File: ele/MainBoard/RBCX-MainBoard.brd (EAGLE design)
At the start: 100 x 100 mm, 449 parts, among them IC1 AMS1117-3.3, IC10 INA180A4, IC11 INA180A4, IC12 MPU-6050, IC13 STM32F103VCT6, IC2 DRV8833PWP, IC3 INA180A4, IC4 INA180A4, IC5 DRV8833PWP, IC6 INA180A4, IC7 INA180A4, IC8 INA180A4, IC9 INA180A4, P1 M1, P2 M2, P3 M3, P4 M4, Q1 NCE20P45Q, Q10 2N7002, Q2 NCE20P45Q, Q3 2N7002, Q4 2N7002, Q5 2N7002, Q6 2N7002, Q7 2N7002, Q8 2N7002, Q9 2N7002, X1 POWER_IN, X2 POWER_OUT, X3 52559-3092, X4 uUSB, Y1 5032/2P, Y2 3215_2P

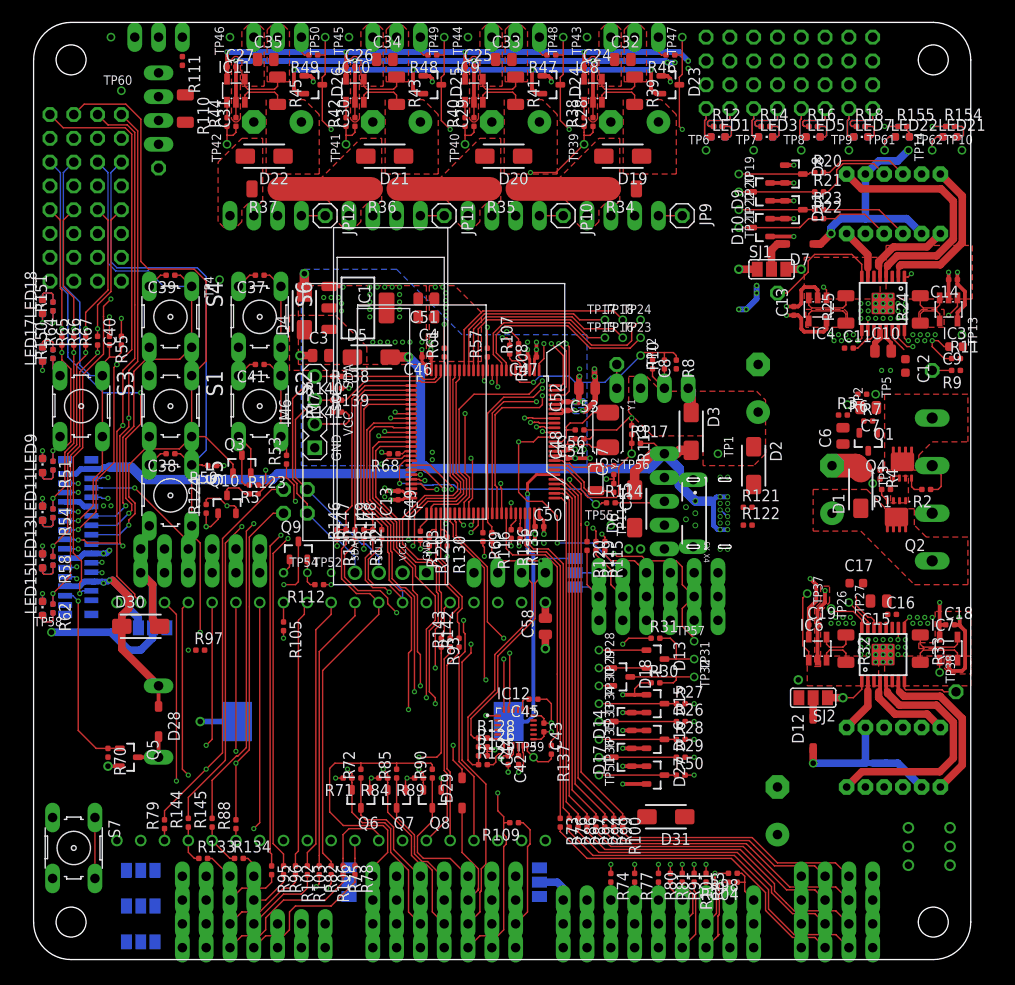
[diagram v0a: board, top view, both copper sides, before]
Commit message: MainBoard: Fix USB connectors, ROUTED
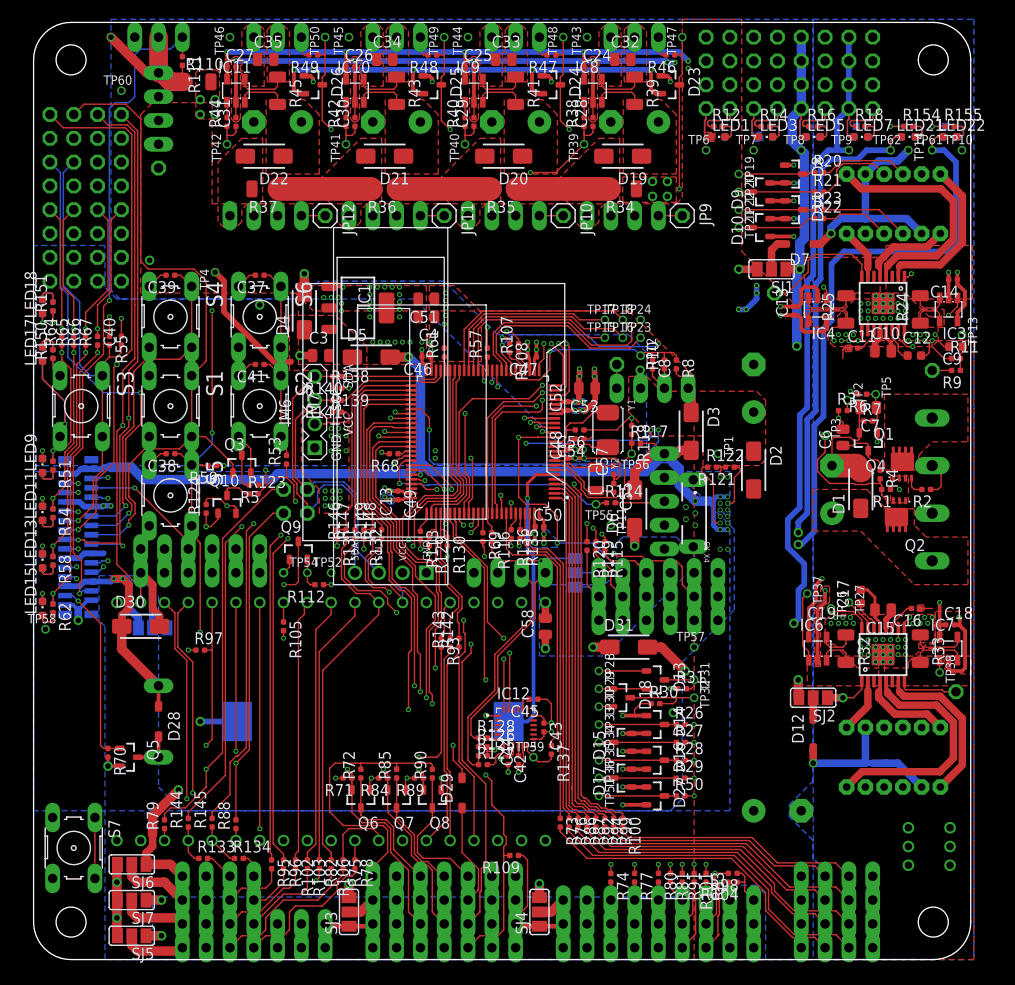
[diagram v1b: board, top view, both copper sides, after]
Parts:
- moved D31 18.5 mm to (63.5, 33.3), turned to 0 degrees
- moved R122 7.27 mm to (72.4, 52.5)
- moved TP3 7.18 mm to (84.5, 55.9)
- moved R31 6.11 mm to (69.2, 28.9)
- moved D15 5.41 mm to (62.9, 23.2), turned to 90 degrees
- moved LED22 5.08 mm to (97.8, 87.8)
- moved LED24 5.08 mm to (97.8, 87.8)
- moved R155 5.08 mm to (97.8, 88.9)
- moved R157 5.08 mm to (97.8, 88.9)
- moved TP61 5.08 mm to (95.9, 86.4)
- moved R121 4.69 mm to (74.3, 52.5), turned to 180 degrees
- moved LED21 4.45 mm to (93.3, 87.8)
- moved LED23 4.45 mm to (93.3, 87.8)
- moved R154 4.45 mm to (93.3, 88.9)
- moved R156 4.45 mm to (93.3, 88.9)
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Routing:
- net +3V3S: track 394.7 -> 538.3 mm, vias 74 -> 97
- net +3V3: track 42.0 -> 134.6 mm, vias 5 -> 8
- net GND_SEPARATOR: track 0.00 -> 83.5 mm
- net ESP_+5V: track 6.28 -> 86.1 mm, vias 2 -> 3
- net BUTTON-ON: track 74.5 -> 149.4 mm, vias 1 -> 4
- net VCC: track 11.8 -> 82.1 mm, vias 1 -> 3
- net POWER: track 0.00 -> 64.4 mm, vias 0 -> 3
- net V_BAT/2: track 0.00 -> 59.3 mm, vias 0 -> 2
- net VUSB: track 111.3 -> 168.1 mm, vias 1 -> 2
- net GND: track 534.9 -> 574.7 mm, vias 138 -> 133
- net +5V: track 42.4 -> 61.8 mm, vias 5 -> 18
- net ILED_PWR: track 0.00 -> 15.7 mm
- net 3V3_IN: track 0.27 -> 14.3 mm
- net BAT+_PROTECTED: track 0.00 -> 12.9 mm, vias 0 -> 1
- net PWRSW_GATE: track 1.45 -> 14.1 mm
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- added copper zone on layer 16, net +3V3
- added copper zone on layer 2, net +3V3
- added copper zone on layer 1, net +5V
- added copper zone on layer 16, net +5V
- added copper zone on layer 2, net ESP-I2C-PWR
- added copper zone on layer 16, net ESP_+5V

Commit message: MainBoardBRD: Fix DRC errors
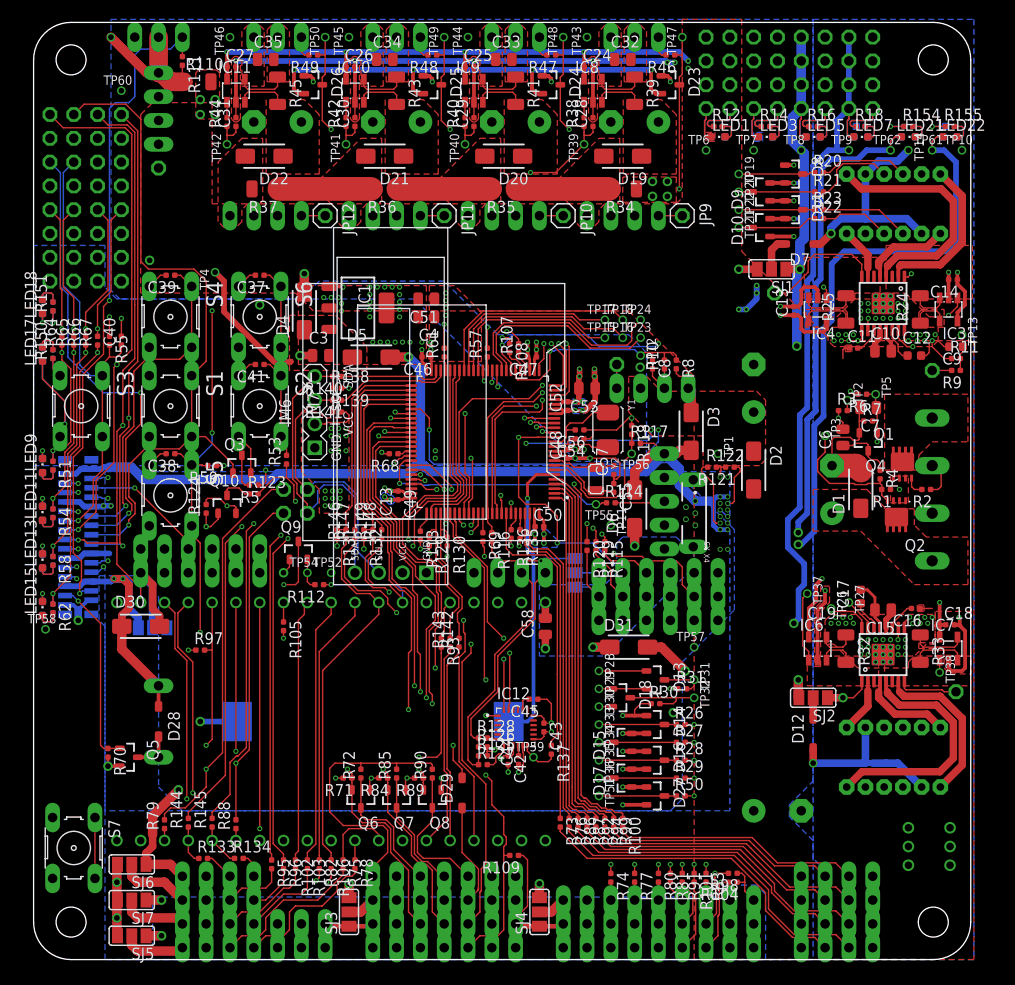
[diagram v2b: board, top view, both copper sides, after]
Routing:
- net GND: track 574.7 -> 558.2 mm
- net GND_SEPARATOR: track 83.5 -> 80.8 mm

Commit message: MainBoardBRD: Add isolation cutout polygon around analog ground vias
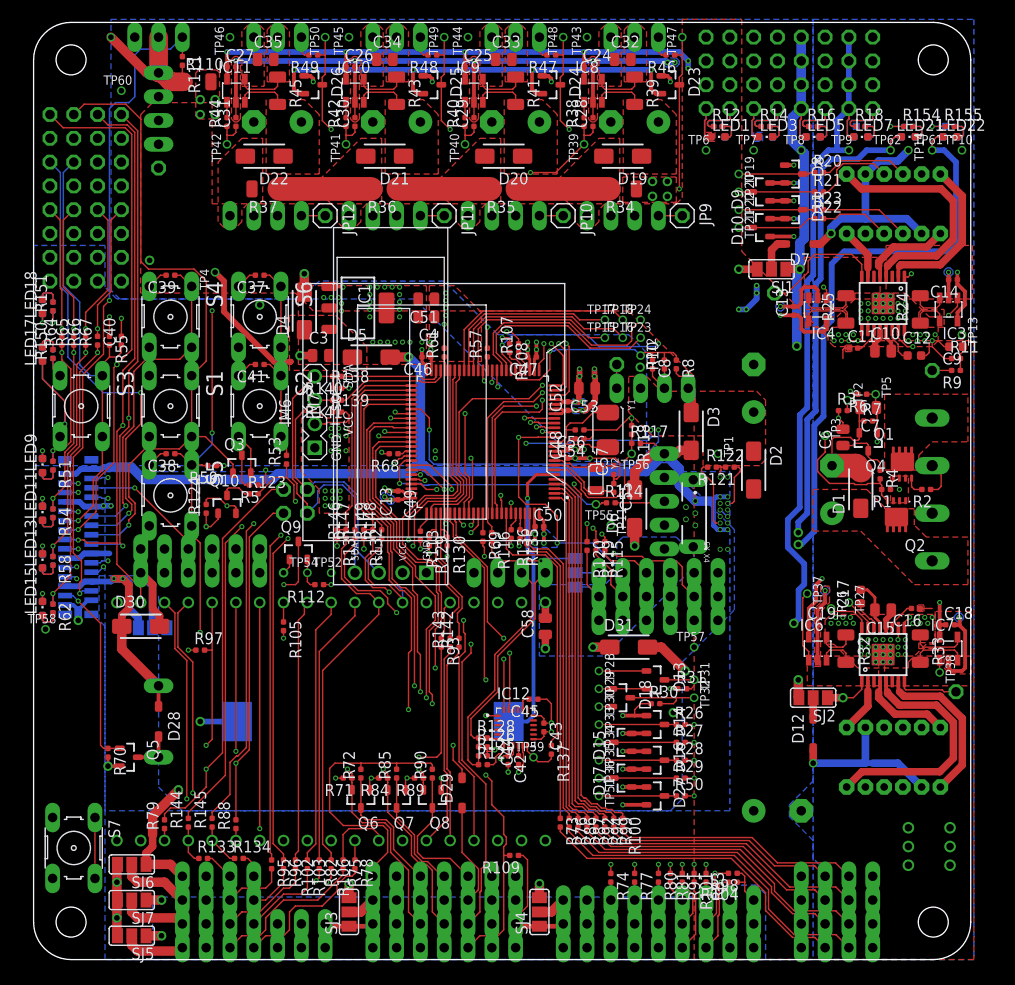
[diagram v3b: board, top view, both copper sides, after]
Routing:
- net +3V3S: track 538.5 -> 539.3 mm
- net VUSB_DET: track 16.5 -> 15.7 mm
- net ENC34PWR: track 18.8 -> 18.0 mm
- net +5V: track 61.8 -> 61.3 mm

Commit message: MainBoardSCH: Reorder sheets and renumber parts
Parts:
- removed C58: 10u, rcl_upravena:C0805
- added C5: 10u, rcl_upravena:C0805
- C10, C32, C33, C34, C35, C7: value 10u -> 1u; device rcl_upravena:C0805 -> rcl_upravena:C0402
- C11: value 10n -> 1u
- C12, C9: value 2u2 -> 1u; device rcl_upravena:C0603 -> rcl_upravena:C0402
- C13: value 100n -> 1u
- C14, C19: value 100n -> 10u; device rcl_upravena:C0402 -> rcl_upravena:C0805
- C15: value 10u -> 10n; device rcl_upravena:C0805 -> rcl_upravena:C0402
- C16: value 10n -> 2u2; device rcl_upravena:C0402 -> rcl_upravena:C0603
- C17: value 2u2 -> 100n; device rcl_upravena:C0603 -> rcl_upravena:C0402
- C20: value 220u -> 10n; device rcl_upravena:E5-10,5 -> rcl_upravena:C0402
- C21: value 220u -> 2u2; device rcl_upravena:E5-10,5 -> rcl_upravena:C0603
- C22, C23: value 220u -> 100n; device rcl_upravena:E5-10,5 -> rcl_upravena:C0402
- C24, C25, C26, C27: value 100n -> 220u; device rcl_upravena:C0402 -> rcl_upravena:E5-10,5
- C28, C29, C30, C31: value 1u -> 100n
- C36: value 220u -> 10u; device rcl_upravena:E5-10,5 -> rcl_upravena:C0805
- C37, C38, C39, C41: value 1u -> 10u; device rcl_upravena:C0402 -> rcl_upravena:C0805
- C40: value 1u -> 220u; device rcl_upravena:C0402 -> rcl_upravena:E5-10,5
- C8: value 1u -> 2u2; device rcl_upravena:C0402 -> rcl_upravena:C0603
- D10, D15, D9: value BAS40-04 -> B5819W; device diode:SOT23 -> diode:SOD123
- D12, D28, D29: value B5819W -> BAS40-04; device diode:SOD123 -> diode:SOT23
- D13, D18: value BAS40-05 -> BAS40-04
- D16: value BAS40-04 -> BAS40-05
- D19, D20, D30: value SS34 -> BAS40-04; device diode:SMA -> diode:SOT23
- D21: value SS34 -> BAS40-05; device diode:SMA -> diode:SOT23
- D23, D24, D25, D8: value BAS40-04 -> SS34; device diode:SOT23 -> diode:SMA
- IM3: value STEPDOWN -> DISPLAY-OLED-128X64-I2C-W_HOLES; device StepDown:STEPDOWN -> diy-modules:DISPLAY-OLED-128X64-I2C_W-HOLES
- IM4: value STEPDOWN -> DISPLAY-OLED-128X32; device StepDown:STEPDOWN -> diy-modules:DISPLAY-OLED-128X32
- IM6: value DISPLAY-OLED-128X64-I2C-W_HOLES -> STEPDOWN; device diy-modules:DISPLAY-OLED-128X64-I2C_W-HOLES -> StepDown:STEPDOWN
- IM7: value DISPLAY-OLED-128X32 -> STEPDOWN; device diy-modules:DISPLAY-OLED-128X32 -> StepDown:STEPDOWN
- JP10: value SERVO2_EN -> ESP_I2C1_5V; device pinhead:1X01 -> pinhead:1X04
- JP11: value SERVO3_EN -> ESP_UART_AUX; device pinhead:1X01 -> pinhead:1X03
- JP12: value SERVO4_EN -> ESP_I2C_AUX1_5V; device pinhead:1X01 -> pinhead:1X03
- JP13: value SERVO1 -> ESP_SPI_AUX1
- JP14: value SERVO2 -> UTS2; device pinhead:1X03 -> pinhead:1X04
- JP15: value SERVO3 -> ESP_I2C2_5V; device pinhead:1X03 -> pinhead:1X04
- JP16: value SERVO4 -> ESP_SPI2; device pinhead:1X03 -> pinhead:1X06
- JP17: value INTELIGENT_SERVO1 -> UTS3; device iServo_connector:292161-3 -> pinhead:1X04
- JP18: value INTELIGENT_SERVO2 -> STM_UART; device iServo_connector:292161-3 -> pinhead:1X04
- JP19: value BUTTONS -> ESP_I2C_AUX2_5V; device pinhead:2X04 -> pinhead:1X03
- JP20: value LEDS -> ESP_SPI_AUX2; device pinhead:2X04 -> pinhead:1X03
- JP21: value PWR_BUTTONS -> UTS4; device pinhead:2X04 -> pinhead:1X04
- JP22: value ESP_UART -> ESP_SPI3; device pinhead:1X04 -> pinhead:1X06
- JP23: value UTS1 -> ESP_I2C1
- JP24: value ESP_SPI1 -> ESP_SPI_AUX3; device pinhead:1X06 -> pinhead:1X03
- JP25: value ESP_I2C1_5V -> ESP_UCOM
- JP26: value ESP_UART_AUX -> ESP_I2C_AUX1
- JP27: value ESP_I2C_AUX1_5V -> ESP_UCOM_AUX
- JP28: value ESP_SPI_AUX1 -> ESP_I2C2; device pinhead:1X03 -> pinhead:1X04
- JP29: value UTS2 -> IM9_EN; device pinhead:1X04 -> pinhead:1X01
- JP30: value ESP_I2C2_5V -> AIO; device pinhead:1X04 -> pinhead:2X04
- JP31: value ESP_SPI2 -> ESP_I2C_AUX2; device pinhead:1X06 -> pinhead:1X03
- JP32: value UTS3 -> ILED; device pinhead:1X04 -> pinhead:1X03
- JP33: value STM_UART -> USB; device pinhead:1X04 -> pinhead:1X05
- JP34: value ESP_I2C_AUX2_5V -> SWD; device pinhead:1X03 -> pinhead:1X06
- JP35: value ESP_SPI_AUX2 -> DEBUG; device pinhead:1X03 -> pinhead:1X04
- JP36: value UTS4 -> BOOT_SW; device pinhead:1X04 -> pinhead:1X02
- JP37: value ESP_SPI3 -> ESP32_JTAG
- JP38: value ESP_I2C1 -> MPU_I2C
- JP39: value ESP_SPI_AUX3 -> EXPANDER_UART; device pinhead:1X03 -> pinhead:1X06
- JP40: value ESP_UCOM -> ESP_PROG_UART
- JP41: value ESP_I2C_AUX1 -> EXPANDER_CAN/I2C; device pinhead:1X03 -> pinhead:1X06
- JP42: value ESP_UCOM_AUX -> BUTTONS; device pinhead:1X03 -> pinhead:2X04
- JP43: value ESP_I2C2 -> LEDS; device pinhead:1X04 -> pinhead:2X04
- JP44: value IM9_EN -> PWR_BUTTONS; device pinhead:1X01 -> pinhead:2X04
- JP45: value AIO -> M12FAULT; device pinhead:2X04 -> pinhead:1X01
- JP46: value ESP_I2C_AUX2 -> M34FAULT; device pinhead:1X03 -> pinhead:1X01
- JP47: value ILED -> SERVO1_EN; device pinhead:1X03 -> pinhead:1X01
- JP48: value USB -> SERVO2_EN; device pinhead:1X05 -> pinhead:1X01
- JP49: value SWD -> SERVO3_EN; device pinhead:1X06 -> pinhead:1X01
- JP50: value DEBUG -> SERVO4_EN; device pinhead:1X04 -> pinhead:1X01
- JP51: value BOOT_SW -> SERVO1; device pinhead:1X02 -> pinhead:1X03
- JP52: value ESP32_JTAG -> SERVO2; device pinhead:1X06 -> pinhead:1X03
- JP53: value MPU_I2C -> SERVO3; device pinhead:1X04 -> pinhead:1X03
- JP54: value EXPANDER_UART -> SERVO4; device pinhead:1X06 -> pinhead:1X03
- JP55: value ESP_PROG_UART -> INTELIGENT_SERVO1; device pinhead:1X04 -> iServo_connector:292161-3
- JP56: value EXPANDER_CAN/I2C -> INTELIGENT_SERVO2; device pinhead:1X06 -> iServo_connector:292161-3
- JP7: value M12FAULT -> ESP_UART; device pinhead:1X01 -> pinhead:1X04
- JP8: value M34FAULT -> UTS1; device pinhead:1X01 -> pinhead:1X04
- JP9: value SERVO1_EN -> ESP_SPI1; device pinhead:1X01 -> pinhead:1X06
- LED10, LED9: value green -> red
- LED11, LED12: value yellow -> red
- LED13, LED14: value red -> green
- LED15, LED16: value blue -> yellow
- LED19, LED20: value red -> blue
- R104, R98: value 100k -> 330R
- R109: value 4k7 -> 100k
- R110, R37: value 0R -> 4k7; device rcl_upravena:R1206 -> rcl_upravena:R0402
- R112, R113, R132, R134, R136, R76, R77: value 330R -> 1k
- R114: value 1k5 -> 2k2
- R115, R116, R120, R140, R141, R142, R143, R144: value 330R -> 2k2
- R117: value 5k6 -> 2k2
- R118: value 10k -> 5m; device rcl_upravena:R0402 -> rcl_upravena:R1206
- R119, R127, R133, R135, R137: value 330R -> 5m; device rcl_upravena:R0402 -> rcl_upravena:R1206
- R121, R122: value 1k -> 2k2
- R123: value 100k -> 2k2
- R124: value 100k -> 10k
- R125, R71: value 4k7 -> 10k
- R126, R139: value 4k7 -> 5m; device rcl_upravena:R0402 -> rcl_upravena:R1206
- R128, R129, R130, R131, R63: value 330R -> 0R; device rcl_upravena:R0402 -> rcl_upravena:R1206
- R138: value 4k7 -> 1k
- R150, R152, R72, R84, R85, R89, R90, R97: value 4k7 -> 330R
- R151, R153, R156, R157, R40, R44: value 1k -> 330R
- R154, R155, R38, R42: value 1k -> 4k7
- R20, R21, R22, R23: value 2k2 -> 1k
- R24, R25, R43: value 5m -> 4k7; device rcl_upravena:R1206 -> rcl_upravena:R0402
- R26, R27, R28, R29, R46, R47, R48, R49: value 2k2 -> 330R
- R30, R31: value 10k -> 330R
- R32, R33, R39, R41, R45: value 5m -> 330R; device rcl_upravena:R1206 -> rcl_upravena:R0402
- R34, R35, R36: value 0R -> 330R; device rcl_upravena:R1206 -> rcl_upravena:R0402
- R50: value 2k2 -> 4k7
- R51, R57, R74, R75: value 330R -> 100k
- R62, R64, R78, R79: value 330R -> 4k7
- R67: value 330R -> 1k5
- R70: value 100k -> 5k6
- moved JP32 117.1 mm to (13.3, 98.4), turned to 0 degrees
- moved JP21 113.3 mm to (85.7, 8.89)
- moved JP29 108.4 mm to (13.3, 84.5), turned to 90 degrees
- moved LED11 104.8 mm to (97.8, 87.8), turned to 270 degrees
- moved LED12 104.8 mm to (97.8, 87.8), turned to 90 degrees
- moved JP20 101.7 mm to (74.3, 3.81)
- moved TP46 101.6 mm to (96.7, 30.6), turned to 270 degrees
- moved JP16 101.5 mm to (62.9, 3.81), turned to 180 degrees
- moved JP14 100.6 mm to (85.7, 3.81), turned to 180 degrees
- moved LED22 99.6 mm to (0.95, 64.6), flipped to the bottom, turned to 0 degrees
- moved LED10 98.8 mm to (93.3, 87.8), turned to 90 degrees
- moved LED9 98.8 mm to (93.3, 87.8), turned to 270 degrees
- moved LED24 98.5 mm to (0.95, 69.7), turned to 0 degrees
- moved LED21 95.3 mm to (0.95, 64.6), turned to 0 degrees
- moved LED23 94.1 mm to (0.95, 69.7), flipped to the top, turned to 0 degrees
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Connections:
- net !M12_FAULT: now also JP45.1; no longer JP7.1
- net !M34_FAULT: now also JP46.1; no longer JP8.1
- net +3V3: now also JP11.3, JP13.3, JP16.1, JP20.3, JP22.1, JP23.1, JP24.3, JP27.3, JP28.1, JP31.3, JP37.5, Q5.1, R24.2, R37.2, R42.2, R50.1, R51.1, R57.1, R62.1, SJ1.1, SJ2.1, TP10.P$1; no longer JP28.3, JP31.1, JP35.3, JP37.1, JP38.1, JP39.3, JP41.3, JP42.3, JP43.1, JP46.3, JP52.5, Q8.1, R104.1, R109.1, R71.2, R84.2, R89.2, R97.1, R98.1, SJ4.1, SJ7.1, TP9.P$1
- net +3V3S: now also C17.1, C22.1, C23.1, C28.1, C29.1, C30.1, C31.1, D12.2, D13.2, D18.2, D19.2, D20.2, D28.2, D29.2, D30.2, IM3.2, IM4.2, JP30.5, JP30.6, JP34.1, JP35.1, JP36.1, JP38.1, JP40.1, LED23.A, LED24.A, Q8.1, R154.2, R155.2, R78.2, R79.2, SJ4.1, SJ7.1, SJ8.1, TP9.P$1; no longer C13.1, C14.1, C19.1, C24.1, C25.1, C26.1, C27.1, D10.2, D15.2, D16.2, D23.2, D24.2, D25.2, D8.2, D9.2, IM6.2, IM7.2, JP45.5, JP45.6, JP49.1, JP50.1, JP51.1, JP53.1, JP55.1, LED18.A, LED20.A, Q9.1, R125.2, R126.2, R138.2, R139.2, SJ1.1, SJ2.1, SJ6.1, TP8.P$1
- net +5V: now also D8.C, D9.C, JP14.1, JP17.1, JP21.1, JP30.7, JP30.8, JP8.1, R128.1, R63.2, SJ8.3, TP8.P$1; no longer D28.C, D30.C, JP23.1, JP29.1, JP32.1, JP36.1, JP45.7, JP45.8, R110.2, R34.1, SJ6.3, TP7.P$1
- net BOOT0: now also JP36.2, Q9.1, R75.1, TP19.P$1; no longer JP51.2, Q10.1, R124.1, TP57.P$1
- net BOOT1_PULL-DOWN: now also Q9.3, R74.1; no longer Q10.3, R123.1
- net BUTTON-1: now also C13.1, JP42.1, R92.2; no longer C41.1, JP19.1, R53.2
- net BUTTON-2: now also C12.1, JP42.3, R94.2; no longer C40.1, JP19.3, R55.2
- net BUTTON-3: now also C11.1, JP42.5, R96.2; no longer C39.1, JP19.5, R57.2
- net BUTTON-4: now also C10.1, JP42.7, R98.2; no longer C38.1, JP19.7, R59.2
- net BUTTON-OFF: now also C9.1, JP44.1, R100.2; no longer C37.1, JP21.1, R61.2
- net BUTTON-ON: now also C5.2, JP44.3; no longer C6.2, JP21.3
- net BUTTON1: now also R74.2, R92.1; no longer R123.2, R53.1
- net BUTTON2: now also R94.1; no longer R55.1
- net BUTTON3: now also R96.1; no longer R57.1
- net BUTTON4: now also R98.1; no longer R59.1
- net BUTTON_OFF: now also R100.1; no longer R61.1
- net BUZZER: now also R108.1; no longer R69.1
- net BUZZER-: now also D9.A, Q10.3; no longer D28.A, Q5.3
- net BUZZER-GATE: now also Q10.1, R108.2, R109.1, TP21.P$1; no longer Q5.1, R69.2, R70.1, TP52.P$1
- net DEBUG-RX: now also JP35.3, R72.2; no longer JP50.3, R119.2
- net DEBUG-TX: now also JP35.4, R73.2, SJ6.1; no longer JP50.4, R120.2, SJ8.1
- net DEBUG_RX: now also R72.1; no longer R119.1
- net DEBUG_TX: now also R73.1; no longer R120.1
- net ENC12PWR: now also D10.C, TP22.P$1; no longer D7.C, TP14.P$1
- net ENC12_PWR: now also D10.A, SJ8.2; no longer D7.A, SJ1.2
- net ENC1A: now also D12.3, R115.1, TP28.P$1; no longer D8.3, R20.1, TP19.P$1
- net ENC1B-SWO: now also R69.2, SJ6.3; no longer R116.2, SJ8.3
- net ENC1B/SWO: now also D11.3, R114.1, R69.1, TP27.P$1; no longer D9.3, R116.1, R21.1, TP20.P$1
- net ENC2A: now also D14.3, R117.1, TP30.P$1; no longer D10.3, R22.1, TP21.P$1
- net ENC2B: now also D13.3, R116.1, TP29.P$1; no longer D11.3, R23.1, TP22.P$1
- net ENC34PWR: now also D15.C, TP33.P$1; no longer D12.C, TP25.P$1
- net ENC34_PWR: now also D15.A, SJ9.2; no longer D12.A, SJ2.2
- net ENC3A: now also D17.3, R120.1, TP41.P$1; no longer D14.3, R26.1, TP33.P$1
- net ENC3B: now also D18.3, R121.1, TP42.P$1; no longer D15.3, R27.1, TP34.P$1
- net ENC4A: now also D19.3, R122.1, TP43.P$1; no longer D16.3, R28.1, TP35.P$1
- net ENC4B: now also D20.3, R123.1, TP44.P$1; no longer D17.3, R29.1, TP36.P$1
- net ENC_1A: now also R115.2; no longer R20.2
- net ENC_1B: now also R114.2; no longer R21.2
- net ENC_2A: now also R117.2; no longer R22.2
- net ENC_2B: now also R116.2; no longer R23.2
- net ENC_3A: now also R120.2; no longer R26.2
- net ENC_3B: now also R121.2; no longer R27.2
- net ENC_4A: now also R122.2; no longer R28.2
- net ENC_4B: now also R123.2; no longer R29.2
- net ESP-EN: now also JP44.5, R107.2; no longer JP21.5, R68.2
- net ESP-I2C-PWR: now also JP10.1, JP12.3, JP15.1, JP19.3, R25.2, R38.2, R43.2, SJ1.2; no longer JP25.1, JP27.3, JP30.1, JP34.3, R72.2, R85.2, R90.2, SJ3.2
- net ESP-I2C-SCL: now also JP23.3, JP28.3, Q5.2, R24.1, R32.2; no longer JP38.3, JP43.3, Q6.2, R71.1, R79.2
- net ESP-I2C-SCL-5V: now also JP10.3, JP15.3, Q5.3, R25.1; no longer JP25.3, JP30.3, Q6.3, R72.1
- net ESP-I2C-SDA: now also JP23.4, JP28.4, Q6.2, R37.1, R41.2; no longer JP38.4, JP43.4, Q7.2, R84.1, R88.2
- net ESP-I2C-SDA-5V: now also JP10.4, JP15.4, Q6.3, R38.1; no longer JP25.4, JP30.4, Q7.3, R85.1
- net ESP-SPI-!CS1: now also JP9.6, R34.2; no longer JP24.6, R81.2
- net ESP-SPI-!CS2: now also JP16.6, R44.2; no longer JP31.6, R91.2
- net ESP-SPI-!CS3: now also JP22.6, R54.2; no longer JP37.6, R101.2
- net ESP-SPI-MISO: now also JP16.4, JP22.4, JP9.4, R30.2; no longer JP24.4, JP31.4, JP37.4, R77.2
- net ESP-SPI-MOSI: now also JP16.3, JP22.3, JP9.3, R27.2; no longer JP24.3, JP31.3, JP37.3, R74.2
- net ESP-SPI-SCK: now also JP16.5, JP22.5, JP9.5, R33.2; no longer JP24.5, JP31.5, JP37.5, R80.2
- net ESP-UART-RX: now also JP40.4, R87.2; no longer JP55.4, R134.2
- net ESP-UART-TX: now also JP40.3, R86.2; no longer JP55.3, R133.2
- net ESP-USART-RX: now also JP7.3, R28.2; no longer JP22.3, R75.2
- net ESP-USART-TX: now also JP7.4, R31.2; no longer JP22.4, R78.2
- net ESP_+5V: now also C41.2, LED11.A, LED12.A; no longer C58.2, LED22.A, LED24.A
- net ESP_COM_RX: now also R145.2, R83.1; no longer R130.1, R142.2
- net ESP_COM_TX: now also R146.2, R82.1; no longer R129.1, R143.2
- net ESP_EN: now also R107.1; no longer R68.1
- net ESP_PROG_RX: now also R147.2; no longer R144.2
- net ESP_PROG_TX: now also R148.2; no longer R145.2
- net ESP_SPI_PWR: now also JP9.1, SJ2.2; no longer JP24.1, SJ4.2
- net ESP_UCOM_PWR: now also JP25.1, SJ5.2; no longer JP40.1, SJ7.2
- net ESP_USART_PWR: now also JP7.1, SJ3.2; no longer JP22.1, SJ5.2
- net EXPANDER-COM-DIR: now also JP39.5, JP41.5, R84.2; no longer JP54.5, JP56.5, R131.2
- net EXPANDER-COM-INT: now also JP39.6, JP41.6, R85.2; no longer JP54.6, JP56.6, R132.2
- net EXPANDER-UART-RX: now also JP39.4, R83.2; no longer JP54.4, R130.2
- net EXPANDER-UART-TX: now also JP39.3, R82.2; no longer JP54.3, R129.2
- net EXPANDER_COM_PWR: now also D8.A, JP39.1, JP41.1, SJ7.2, TP20.P$1; no longer D30.A, JP54.1, JP56.1, SJ9.2, TP58.P$1
- net EXPANDER_RX: now also R146.1; no longer R143.1
- net EXPANDER_TX: now also R145.1; no longer R142.1
- net GND: now also C11.2, C16.2, C21.2, C22.2, C23.2, C24.-, C25.-, C26.-, C27.-, C32.2, C33.2, C34.2, C35.2, C36.1, C37.1, C38.1, C39.1, C40.-, C41.1, C6.2, D12.1, D13.1, D18.1, D19.1, D20.1, D28.1, D29.1, D30.1, IM3.1, IM4.1, IM6.GND, IM7.GND, JP10.2, JP11.2, JP12.2, JP13.2, JP14.4, JP15.2, JP16.2, JP17.4, JP18.2, JP23.2, JP30.3, JP30.4, JP32.3, JP33.5, JP34.3, JP37.6, JP42.4, JP42.6, JP42.8, JP43.4, JP43.6, JP43.8, JP44.2, JP44.4, JP44.6, JP44.8, JP51.3, JP52.3, JP53.3, JP54.3, JP55.3, JP56.3, JP7.2, JP8.4, JP9.2, LED17.C, LED18.C, LED19.C, LED20.C, Q9.2, R109.2, R110.1, R111.1, R112.1, R113.1, R119.1, R124.1, R125.1, R126.1, R127.1, R20.1, R21.1, R22.1, R23.1, R71.1, R75.2, R76.2, R77.2, TP11.P$1; no longer C15.2, C20.-, C21.-, C22.-, C23.-, C24.2, C25.2, C26.2, C27.2, C32.1, C33.1, C34.1, C35.1, C36.-, C37.2, C38.2, C39.2, C40.2, C41.2, C58.1, D10.1, D15.1, D16.1, D23.1, D24.1, D25.1, D8.1, D9.1, IM3.GND, IM4.GND, IM6.1, IM7.1, JP13.3, JP14.3, JP15.3, JP16.3, JP17.3, JP18.3, JP19.4, JP19.6, JP19.8, JP20.4, JP20.6, JP20.8, JP21.2, JP21.6, JP21.8, JP23.4, JP29.4, JP30.2, JP32.4, JP33.2, JP34.2, JP36.4, JP37.2, JP45.3, JP45.4, JP46.2, JP47.3, JP48.5, JP49.3, JP50.2, JP52.6, JP53.2, JP54.2, JP55.2, JP56.2, LED10.C, LED11.C, LED12.C, LED9.C, Q5.2, R121.2, R122.2, R124.2, R150.1, R151.1, R152.1, R153.1, R154.1, R155.1, R156.1, R157.1, R24.1, R25.1, R30.1, R31.1, R32.1, R33.1, R70.2, TP10.P$1
- net GPIO-1: now also JP13.1, R36.2; no longer JP28.1, R83.2
- net GPIO-1-5V: now also JP12.1, Q7.3, R43.1; no longer JP27.1, Q8.3, R90.1
- net GPIO-2: now also JP26.1, R58.2; no longer JP41.1, R105.2
- net GPIO-3: now also JP25.3, R55.2; no longer JP40.3, R102.2
- net GPIO-4: now also JP25.4, R56.2; no longer JP40.4, R103.2
- net GPIO-5: now also JP11.1, R35.2; no longer JP26.1, R82.2
- net GPIO-6: now also JP27.1, R59.2; no longer JP42.1, R106.2
- net GPIO-7: now also Q7.2, R42.1, R46.2; no longer Q8.2, R89.1, R93.2
- net GPIO1: now also R36.1; no longer R83.1
- net GPIO2: now also R58.1; no longer R105.1
- net GPIO3: now also R55.1; no longer R102.1
- net GPIO4: now also R56.1; no longer R103.1
- net GPIO5: now also R35.1; no longer R82.1
- net GPIO6/TMS: now also JP37.1, R149.1, R59.1; no longer JP52.1, R106.1, R146.1
- net GPIO7/TCK: now also JP37.3, R150.1, R46.1; no longer JP52.3, R147.1, R93.1
- net I2C_SCL: now also R32.1; no longer R79.1
- net I2C_SDA: now also R41.1; no longer R88.1
- net ILED: now also Q8.2, R65.2, TP16.P$1; no longer Q9.2, R112.2, TP54.P$1
- net ILED-5V: now also JP32.1, Q8.3, R64.1; no longer JP47.1, Q9.3, R111.1
- net ILED_PWR: now also IM2.OUT, JP32.2, R63.1, R64.2, TP15.P$1; no longer IM8.OUT, JP47.2, R110.1, R111.2, TP53.P$1
- net IM9_EN: now also IM2.EN, JP29.1; no longer IM8.EN, JP44.1
- net IN1: now also JP20.1, R51.2; no longer JP35.1, R98.2
- net IN2: now also JP24.1, R57.2; no longer JP39.1, R104.2
- net IN3: now also D7.A, R50.2; no longer D29.A, R97.2
- net IN3-5V: now also D7.C, JP19.1; no longer D29.C, JP34.1
- net IN4: now also JP31.1, R62.2; no longer JP46.1, R109.2
- net IN4A: now also D16.1, TP36.P$1; no longer D13.1, TP28.P$1
- net IN4B: now also D21.2, TP38.P$1; no longer D18.2, TP30.P$1
- net IN4_A: now also D16.3, R125.2, TP39.P$1; no longer D13.3, R31.2, TP31.P$1
- net IN4_B: now also D21.3, R124.2, TP40.P$1; no longer D18.3, R30.2, TP32.P$1
- net INTELLIGENT_SERVO: now also D30.3, R144.1, TP59.P$1; no longer D27.3, R50.1, TP51.P$1
- net ISERVO: now also JP55.1, JP56.1, R144.2; no longer JP17.1, JP18.1, R50.2
- net I_LED/TDI: now also JP37.2, R151.1, R65.1; no longer JP52.2, R112.1, R148.1
- net LED-1: now also JP43.1, R103.2; no longer JP20.1, R64.2
- net LED-2: now also JP43.3, R104.2; no longer JP20.3, R65.2
- net LED-3: now also JP43.5, R105.2; no longer JP20.5, R66.2
- net LED-4: now also JP43.7, R106.2; no longer JP20.7, R67.2
- net LED1: now also R103.1, R90.1, R91.1; no longer R51.1, R52.1, R64.1
- net LED2: now also R104.1, R93.1, R95.1; no longer R54.1, R56.1, R65.1
- net LED3: now also R105.1, R97.1, R99.1; no longer R58.1, R60.1, R66.1
- net LED4: now also R101.1, R102.1, R106.1; no longer R62.1, R63.1, R67.1
- net LED_1: now also LED13.A, R90.2; no longer LED9.A, R51.2
- net LED_1B: now also LED14.A, R91.2; no longer LED10.A, R52.2
- net LED_2: now also LED15.A, R93.2; no longer LED11.A, R54.2
- net LED_2B: now also LED16.A, R95.2; no longer LED12.A, R56.2
- net LED_3: now also LED17.A, R97.2; no longer LED13.A, R58.2
- net LED_3B: now also LED18.A, R99.2; no longer LED14.A, R60.2
- net LED_4: now also LED19.A, R101.2; no longer LED15.A, R62.2
- net LED_4B: now also LED20.A, R102.2; no longer LED16.A, R63.2
- net M1GND: now also R118.2; no longer R24.2
- net M2GND: now also R119.2; no longer R25.2
- net M3GND: now also R126.2; no longer R32.2
- net M4GND: now also R127.2; no longer R33.2
- net MI1: now also TP31.P$1; no longer TP23.P$1
- net MI2: now also TP32.P$1; no longer TP24.P$1
- net MI3: now also TP45.P$1; no longer TP37.P$1
- net MI4: now also TP46.P$1; no longer TP38.P$1
- net MPU-INT: now also R153.2, TP62.P$1; no longer R137.2, TP59.P$1
- net MPU-SCL: now also JP38.3, R78.1, R80.1; no longer JP53.3, R125.1, R127.1
- net MPU-SDA: now also JP38.4, R79.1, R81.1; no longer JP53.4, R126.1, R128.1
- net MPU_INT: now also R153.1; no longer R137.1
- net MPU_SCL: now also R80.2; no longer R127.2
- net MPU_SDA: now also R81.2; no longer R128.2
- net NRST: now also JP34.5, JP44.7; no longer JP21.7, JP49.5
- net POWER: now also C6.1, TP6.P$1; no longer C7.1, TP5.P$1
- net PWM1A: now also TP23.P$1; no longer TP15.P$1
- net PWM1B: now also TP24.P$1; no longer TP16.P$1
- net PWM2A: now also TP25.P$1; no longer TP17.P$1
- net PWM2B: now also TP26.P$1; no longer TP18.P$1
- net PWM3A: now also TP34.P$1; no longer TP26.P$1
- net PWM3B: now also TP35.P$1; no longer TP27.P$1
- net PWM4: now also D16.2, D21.1, TP37.P$1; no longer D13.2, D18.1, TP29.P$1
- net PWRLED_+3V3S1: now also LED23.C, R112.2; no longer LED18.C, R151.2
- net PWRLED_+3V3S_B1: now also LED24.C, R113.2; no longer LED20.C, R153.2
- net PWRLED_+5VESP: now also LED11.C, R22.2; no longer LED22.C, R155.2
- net PWRLED_+5VESP_B: now also LED12.C, R23.2; no longer LED24.C, R157.2
- net PWRLED_VCC1: now also LED21.C, R110.2; no longer LED17.C, R150.2
- net PWRLED_VCC_B1: now also LED22.C, R111.2; no longer LED19.C, R152.2
- net PWRLED_VUSB: now also LED9.C, R20.2; no longer LED21.C, R154.2
- net PWRLED_VUSB_B: now also LED10.C, R21.2; no longer LED23.C, R156.2
- net PWRSW: now also C5.1; no longer C6.1
- net SERVO1: now also D26.3, R140.1, TP55.P$1; no longer D23.3, R46.1, TP47.P$1
- net SERVO1PWR: now also D22.A, IM5.OUT, R128.2, R129.1; no longer D19.A, IM2.OUT, R34.2, R35.1
- net SERVO1_EN: now also IM5.EN, JP47.1; no longer IM2.EN, JP9.1
- net SERVO1_PWR: now also C24.+, D22.C, R133.2; no longer C20.+, D19.C, R39.2
- net SERVO2: now also D27.3, R141.1, TP56.P$1; no longer D24.3, R47.1, TP48.P$1
- net SERVO2PWR: now also D23.A, IM6.OUT, R129.2, R130.1; no longer D20.A, IM3.OUT, R35.2, R36.1
- net SERVO2_EN: now also IM6.EN, JP48.1; no longer IM3.EN, JP10.1
- net SERVO2_PWR: now also C25.+, D23.C, R135.2; no longer C21.+, D20.C, R41.2
- net SERVO3: now also D28.3, R142.1, TP57.P$1; no longer D25.3, R48.1, TP49.P$1
- net SERVO3PWR: now also D24.A, IM7.OUT, R130.2, R131.1; no longer D21.A, IM4.OUT, R36.2, R37.1
- net SERVO3_EN: now also IM7.EN, JP49.1; no longer IM4.EN, JP11.1
- net SERVO3_PWR: now also C26.+, D24.C, R137.2; no longer C22.+, D21.C, R43.2
- net SERVO4: now also D29.3, R143.1, TP58.P$1; no longer D26.3, R49.1, TP50.P$1
- net SERVO4PWR: now also D25.A, IM8.OUT, R131.2; no longer D22.A, IM5.OUT, R37.2
- net SERVO4_EN: now also IM8.EN, JP50.1; no longer IM5.EN, JP12.1
- net SERVO4_PWR: now also C27.+, D25.C, R139.2; no longer C23.+, D22.C, R45.2
- net SERVO_1: now also JP51.1, R140.2; no longer JP13.1, R46.2
- net SERVO_1_PWR: now also C36.2, JP51.2, R133.1, TP51.P$1; no longer C32.2, JP13.2, R39.1, TP43.P$1
- net SERVO_2: now also JP52.1, R141.2; no longer JP14.1, R47.2
- net SERVO_2_PWR: now also C37.2, JP52.2, R135.1, TP52.P$1; no longer C33.2, JP14.2, R41.1, TP44.P$1
- net SERVO_3: now also JP53.1, R142.2; no longer JP15.1, R48.2
- net SERVO_3_PWR: now also C38.2, JP53.2, R137.1, TP53.P$1; no longer C34.2, JP15.2, R43.1, TP45.P$1
- net SERVO_4: now also JP54.1, R143.2; no longer JP16.1, R49.2
- net SERVO_4_PWR: now also C39.2, JP54.2, R139.1, TP54.P$1; no longer C35.2, JP16.2, R45.1, TP46.P$1
- net SI1: now also C32.1, R132.1, TP47.P$1; no longer C28.1, R38.1, TP39.P$1
- net SI2: now also C33.1, R134.1, TP48.P$1; no longer C29.1, R40.1, TP40.P$1
- net SI3: now also C34.1, R136.1, TP49.P$1; no longer C30.1, R42.1, TP41.P$1
- net SI4: now also C35.1, R138.1, TP50.P$1; no longer C31.1, R44.1, TP42.P$1
- net SI_1: now also R132.2; no longer R38.2
- net SI_2: now also R134.2; no longer R40.2
- net SI_3: now also R136.2; no longer R42.2
- net SI_4: now also R138.2; no longer R44.2
- net SPI_!SS1: now also R34.1; no longer R81.1
- net SPI_!SS2: now also R44.1; no longer R91.1
- net SPI_!SS3!/TDO: now also JP37.4, R152.1, R54.1; no longer JP52.4, R101.1, R149.1
- net SPI_MISO: now also R30.1; no longer R77.1
- net SPI_MOSI: now also R27.1; no longer R74.1
- net SPI_SCK: now also R33.1; no longer R80.1
- net STM-AIO1: now also JP30.1, R60.2; no longer JP45.1, R107.2
- net STM-AIO2: now also JP30.2, R61.1; no longer JP45.2, R108.1
- net STM-CAN-RX/I2C-SCL: now also JP41.4, R89.2; no longer JP56.4, R136.2
- net STM-CAN-TX/I2C-SDA: now also JP41.3, R88.2; no longer JP56.3, R135.2
- net STM-I2C-SCL: now also IM3.3, IM4.3, R155.1, R157.2; no longer IM6.3, IM7.3, R139.1, R141.2
- net STM-I2C-SDA: now also IM3.4, IM4.4, R154.1, R156.2; no longer IM6.4, IM7.4, R138.1, R140.2
- net STM-UART-RX: now also JP18.4, R49.2; no longer JP33.4, R96.2
- net STM-UART-TX: now also JP18.3, R48.2; no longer JP33.3, R95.2
- net STM_AIO1: now also R60.1; no longer R107.1
- net STM_AIO2: now also R61.2; no longer R108.2
- net STM_CAN_RX/I2C_SCL: now also R89.1; no longer R136.1
- net STM_CAN_TX/I2C_SDA: now also R88.1; no longer R135.1
- net STM_I2C_SCL: now also R157.1; no longer R141.1
- net STM_I2C_SDA: now also R156.1; no longer R140.1
- net STM_SPI_!CS: now also R149.2, R84.1; no longer R131.1, R146.2
- net STM_SPI_MISO: now also R152.2, R85.1; no longer R132.1, R149.2
- net STM_SPI_MOSI: now also R151.2; no longer R148.2
- net STM_SPI_SCK: now also R150.2; no longer R147.2
- net STM_UART_PWR: now also JP18.1, SJ4.2; no longer JP33.1, SJ6.2
- net STM_UART_RX: now also R49.1; no longer R96.1
- net STM_UART_TX: now also R48.1; no longer R95.1
- net SWCLK: now also R66.1; no longer R113.1
- net SWCLK_: now also JP34.2, R66.2; no longer JP49.2, R113.2
- net SWDIO: now also R68.1; no longer R115.1
- net SWDIO_: now also JP34.4, R68.2; no longer JP49.4, R115.2
- net SWO: now also JP34.6, SJ6.2; no longer JP49.6, SJ8.2
- net UART2_RX: now also R28.1; no longer R75.1
- net UART2_TX: now also R31.1; no longer R78.1
- net UART_RX: now also R148.1, R87.1; no longer R134.1, R145.1
- net UART_TX: now also R147.1, R86.1; no longer R133.1, R144.1
- net USB_CC1: now also R77.1; no longer R122.1
- net USB_CC2: now also R76.1; no longer R121.1
- net USB_DM: now also JP33.2; no longer JP48.2
- net USB_DP: now also JP33.3, R67.2; no longer JP48.3, R114.2
- net USB_DP_PULLUP: now also R67.1, TP17.P$1; no longer R114.1, TP55.P$1
- net USB_ID: now also JP33.4; no longer JP48.4
- net UTS1-ECHO: now also JP8.3, R29.2; no longer JP23.3, R76.2
- net UTS1-TRIG: now also JP8.2, R26.2; no longer JP23.2, R73.2
- net UTS1_ECHO: now also R29.1; no longer R76.1
- net UTS1_TRIG: now also R26.1; no longer R73.1
- net UTS2-ECHO: now also JP14.3, R40.2; no longer JP29.3, R87.2
- net UTS2-TRIG: now also JP14.2, R39.2; no longer JP29.2, R86.2
- net UTS2_ECHO: now also R40.1; no longer R87.1
- net UTS2_TRIG: now also R39.1; no longer R86.1
- net UTS3-ECHO: now also JP17.3, R47.2; no longer JP32.3, R94.2
- net UTS3-TRIG: now also JP17.2, R45.2; no longer JP32.2, R92.2
- net UTS3_ECHO: now also R47.1; no longer R94.1
- net UTS3_TRIG: now also R45.1; no longer R92.1
- net UTS4-ECHO: now also JP21.3, R53.2; no longer JP36.3, R100.2
- net UTS4-TRIG: now also JP21.2, R52.2; no longer JP36.2, R99.2
- net UTS4_ECHO: now also R53.1; no longer R100.1
- net UTS4_TRIG: now also R52.1; no longer R99.1
- net VBAT: now also TP12.P$1; no longer TP11.P$1
- net VCC: now also C14.1, C19.1, C20.1, C40.+, IM6.IN, IM7.IN, JP55.2, JP56.2, LED21.A, LED22.A, TP7.P$1; no longer C10.1, C11.1, C16.1, C36.+, IM3.IN, IM4.IN, JP17.2, JP18.2, LED17.A, LED19.A, TP6.P$1
- net VCP12: now also C15.2; no longer C11.2
- net VCP34: now also C20.2; no longer C16.2
- net VINT12: now also C16.1; no longer C12.1
- net VINT34: now also C21.1; no longer C17.1
- net VUSB: now also JP33.1, LED10.A, LED9.A, R70.2, TP5.P$1; no longer JP48.1, LED21.A, LED23.A, R117.2, TP62.P$1
- net VUSB_DET: now also R70.1, R71.2, TP18.P$1; no longer R117.1, R118.2, TP56.P$1
- net V_BAT: now also C7.1, TP13.P$1; no longer C8.1, TP12.P$1
- net V_BAT/2: now also C8.1, TP14.P$1; no longer C9.1, TP13.P$1

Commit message: MainBoard: Fix microUSB pinout, add some tSilk
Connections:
- net USB_DM: now also X4.2; no longer X4.3
- net USB_DP: now also X4.3; no longer X4.2
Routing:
- net USB_DP: track 80.5 -> 82.3 mm
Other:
- board text added: "!CS"
- board text added: "+"
- board text added: "-"
- board text added: "3V3"
- board text added: "3V3S"
- board text added: "5V"
- board text added: "5V ESP"
- board text added: "AUX"
- board text added: "B1"
- board text added: "B2"
- board text added: "B3"
- board text added: "B4"
- board text added: "E1+"
- board text added: "E1-"
- board text added: "E1A"
- board text added: "E1B"
- board text added: "E2+"
- board text added: "E2-"
- board text added: "E2A"
- board text added: "E2B"
- board text added: "E3+"
- board text added: "E3-"
- board text added: "E3A"
- board text added: "E3B"
- board text added: "E4+"
- board text added: "E4-"
- board text added: "E4A"
- board text added: "E4B"
- board text added: "ECHO"
- board text added: "ENC12PWR"
- board text added: "GND"
- board text added: "GPIO1 IN1 IN2 !CS1! !CS2! !CS3!"
- board text added: "L1"
- board text added: "L2"
- board text added: "L3"
- board text added: "L4"
- board text added: "M1A"
- board text added: "M1B"
- board text added: "M2A"
- board text added: "M2B"
- board text added: "M3A"
- board text added: "M3B"
- board text added: "M4A"
- board text added: "M4B"
- board text added: "MISO"
- board text added: "MOSI"
- board text added: "OFF ESCAPE"
- board text added: "ON"
- board text added: "ON ENTER"
- board text added: "PWR"
- board text added: "RESET"
- board text added: "SCK"
- board text added: "SEL"
- board text added: "TRIG"
- board text added: "U1"
- board text added: "U2"
- board text added: "U3"
- board text added: "U4"
- board text added: "VCC"
- board text added: "VUSB"
- board text added: "iSERVO"
- board text removed: "1"
- board text removed: "2"
- board text removed: "3"
- board text removed: "4"
- board text removed: "F"
- board text removed: "O"
